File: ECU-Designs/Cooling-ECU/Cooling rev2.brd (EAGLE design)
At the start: 66.3 x 41.9 mm, 17 parts, among them T1 N-CHANNEL_MOSFETGENERIC, T2 N-CHANNEL_MOSFETGENERIC, T3 N-CHANNEL_MOSFETGENERIC, X1 MINIFIT_5566-12

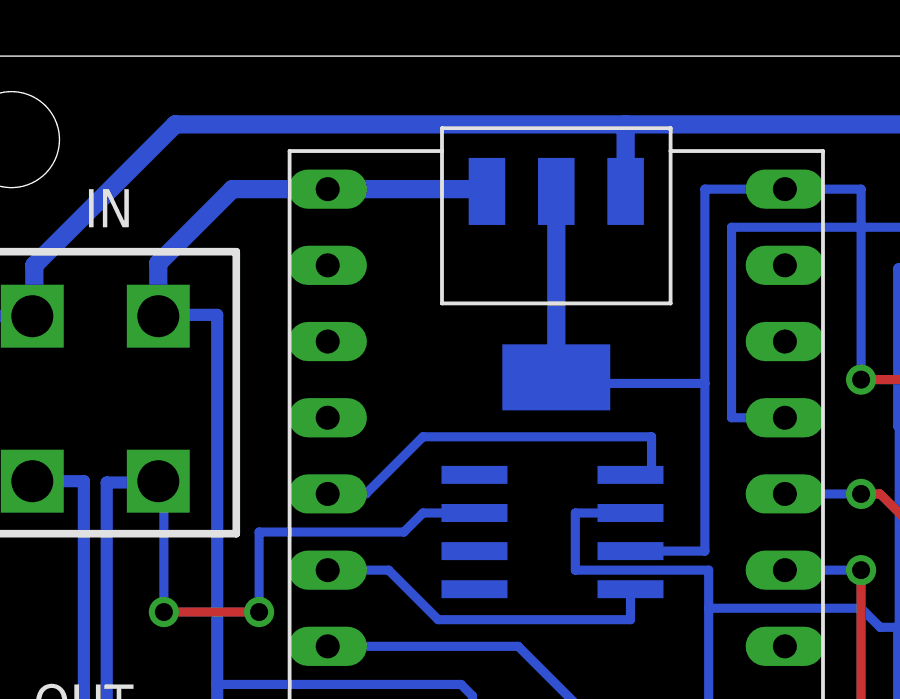
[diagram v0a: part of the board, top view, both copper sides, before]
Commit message: Tried milling out cooling board
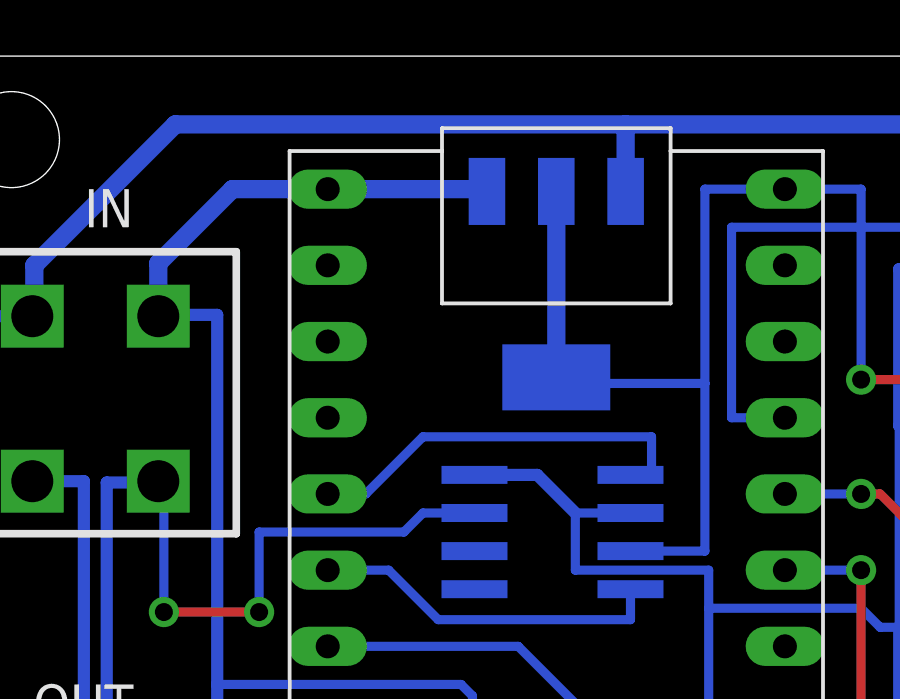
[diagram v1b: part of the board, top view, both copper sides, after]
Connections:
- net GND: now also U$2.8
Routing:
- net GND: track 194.4 -> 198.3 mm
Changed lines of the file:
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@@
 <?xml version="1.0" encoding="utf-8"?>
 <!DOCTYPE eagle SYSTEM "eagle.dtd">
-<eagle version="7.6.0">
+<eagle version="7.2.0">
 <drawing>
 <settings>
@@
 <wire x1="32.385" y1="34.798" x2="33.655" y2="34.798" width="0.4064" layer="16"/>
 <wire x1="33.655" y1="34.798" x2="33.655" y2="34.8996" width="0.4064" layer="16"/>
-<wire x1="13.335" y1="37.465" x2="13.97" y2="37.465" width="0.6096" layer="16"/>
-<wire x1="13.97" y1="37.465" x2="18.6436" y2="37.465" width="0.6096" layer="16"/>
+<wire x1="13.335" y1="37.465" x2="18.6436" y2="37.465" width="0.6096" layer="16"/>
 <wire x1="18.6436" y1="37.465" x2="18.6436" y2="37.3888" width="0.6096" layer="16"/>
 <wire x1="7.688" y1="16.72" x2="9.608" y2="16.72" width="0.4064" layer="16"/>
@@
 <wire x1="7.688" y1="34.993" x2="10.16" y2="37.465" width="0.6096" layer="16"/>
 <wire x1="10.16" y1="37.465" x2="13.335" y2="37.465" width="0.6096" layer="16"/>
+<contactref element="U$2" pad="8"/>
+<wire x1="18.228" y1="27.94" x2="20.32" y2="27.94" width="0.4064" layer="16"/>
+<wire x1="20.32" y1="27.94" x2="21.59" y2="26.67" width="0.4064" layer="16"/>
 </signal>
 <signal name="N$2">

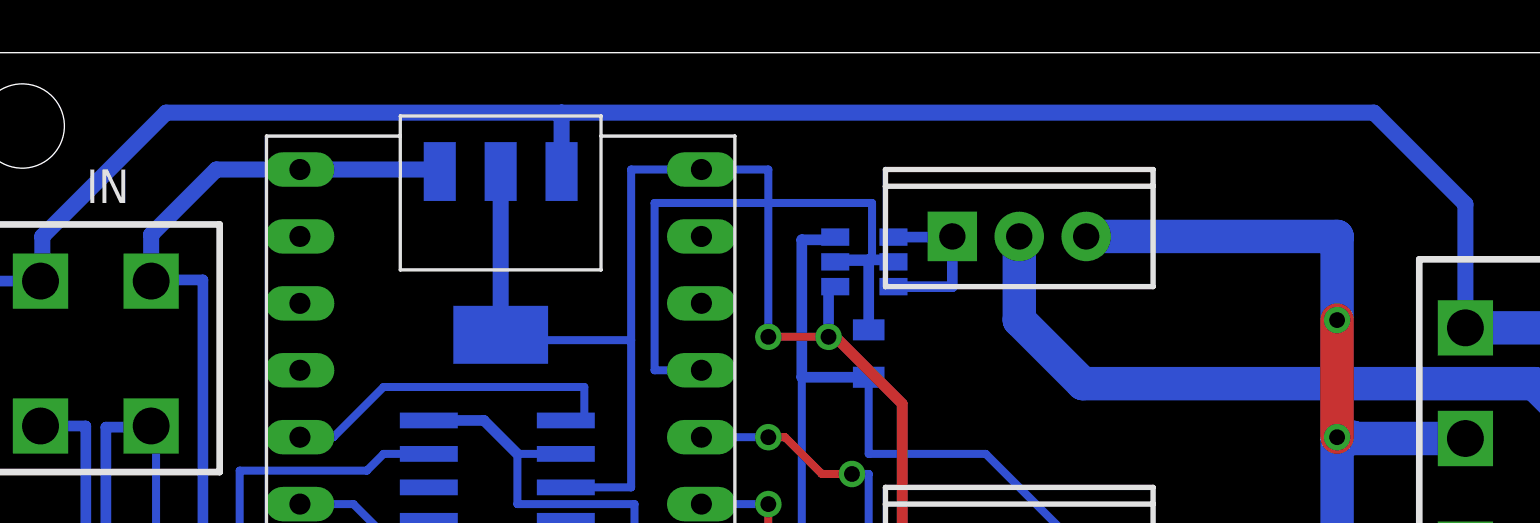
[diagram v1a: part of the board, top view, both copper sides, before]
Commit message: Nathan screwed up the package so we had to blow stuff up
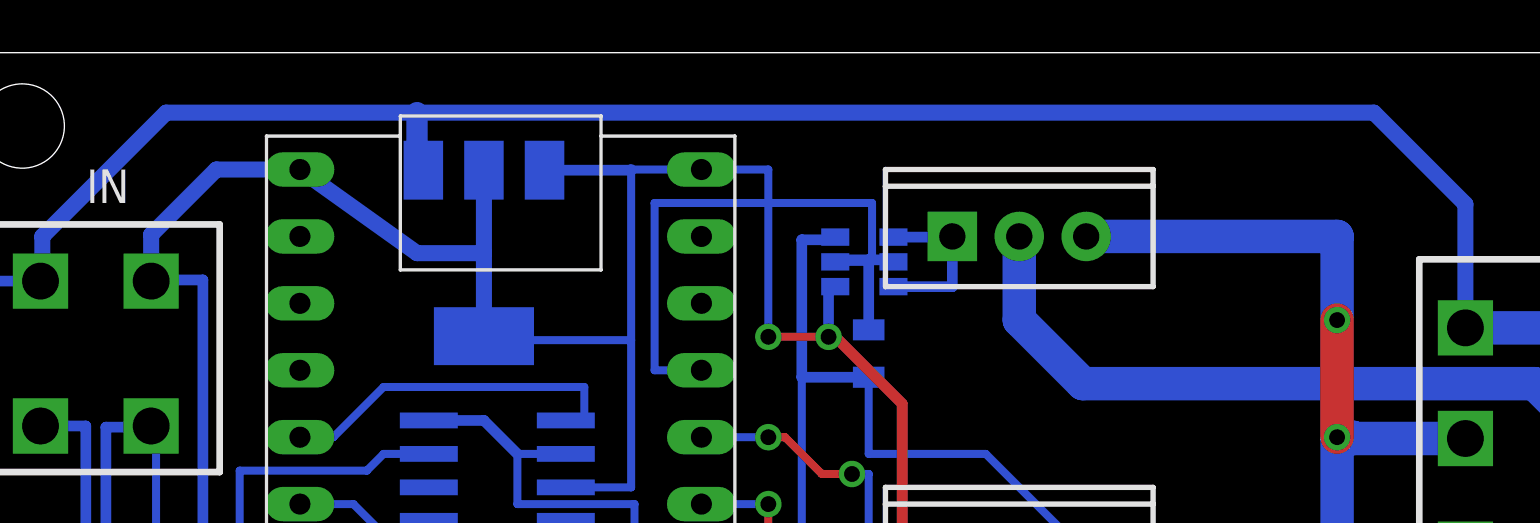
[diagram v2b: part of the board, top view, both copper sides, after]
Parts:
- removed 5V_REG: (no value), HyTechDevices:SOT223
- added U$4: (no value), HyTechDevices:SOT223
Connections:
- net +12V: now also U$4.1; no longer 5V_REG.3
- net +5V: now also U$4.3; no longer 5V_REG.2, 5V_REG.4
- net GND: now also U$4.2, U$4.4; no longer 5V_REG.1
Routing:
- net GND: track 198.3 -> 207.3 mm
- net +5V: track 119.2 -> 116.0 mm
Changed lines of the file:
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@@
 </autorouter>
 <elements>
-<element name="5V_REG" library="HyTechDevices" package="SOT223" value="" x="20.955" y="34.29" rot="MR180"/>
 <element name="IN" library="HyTechDevices" package="MINIFIT_5566-4" value="MINIFIT_5566-4" x="5.588" y="30.48" rot="R180">
 <attribute name="OC_FARNELL" value="unknown" x="5.588" y="30.48" size="1.778" layer="27" rot="R180" display="off"/>
@@
 <element name="G2" library="HyTechDevices" package="SOT23-6" value="GATE_DRIVEZXGD3003E6TA" x="33.655" y="20.955" rot="MR90"/>
 <element name="G3" library="HyTechDevices" package="SOT23-6" value="GATE_DRIVEZXGD3003E6TA" x="33.655" y="8.89" rot="MR90"/>
+<element name="U$4" library="HyTechDevices" package="SOT223" value="" x="20.32" y="34.29" rot="MR180"/>
 </elements>
 <signals>
 <signal name="GND">
-<contactref element="5V_REG" pad="1"/>
 <contactref element="IN" pad="2"/>
 <contactref element="OUT" pad="2"/>
@@
 <wire x1="32.385" y1="34.798" x2="33.655" y2="34.798" width="0.4064" layer="16"/>
 <wire x1="33.655" y1="34.798" x2="33.655" y2="34.8996" width="0.4064" layer="16"/>
-<wire x1="13.335" y1="37.465" x2="18.6436" y2="37.465" width="0.6096" layer="16"/>
-<wire x1="18.6436" y1="37.465" x2="18.6436" y2="37.3888" width="0.6096" layer="16"/>
+<wire x1="13.335" y1="37.465" x2="17.78" y2="34.29" width="0.6096" layer="16"/>
 <wire x1="7.688" y1="16.72" x2="9.608" y2="16.72" width="0.4064" layer="16"/>
 <wire x1="9.608" y1="16.72" x2="9.652" y2="16.764" width="0.4064" layer="16"/>
@@
 <wire x1="18.228" y1="27.94" x2="20.32" y2="27.94" width="0.4064" layer="16"/>
 <wire x1="20.32" y1="27.94" x2="21.59" y2="26.67" width="0.4064" layer="16"/>
+<contactref element="U$4" pad="4"/>
+<contactref element="U$4" pad="2"/>
+<wire x1="17.78" y1="34.29" x2="20.32" y2="34.29" width="0.6096" layer="16"/>
+<wire x1="20.32" y1="34.29" x2="20.32" y2="31.14" width="0.6096" layer="16"/>
+<wire x1="20.32" y1="34.29" x2="20.32" y2="37.44" width="0.6096" layer="16"/>
 </signal>
 <signal name="N$2">
@@
 </signal>
 <signal name="+5V">
-<contactref element="5V_REG" pad="2"/>
-<contactref element="5V_REG" pad="4"/>
 <contactref element="U$2" pad="3"/>
 <contactref element="U$3" pad="16"/>
@@
 <via x="33.401" y="6.604" extent="1-16" drill="0.6"/>
 <wire x1="33.655" y1="19.05" x2="33.655" y2="20.955" width="0.4064" layer="16"/>
-<wire x1="20.955" y1="31.191" x2="20.955" y2="37.3888" width="0.6096" layer="16"/>
 <wire x1="28.575" y1="37.465" x2="25.908" y2="37.465" width="0.3048" layer="16"/>
 <wire x1="25.908" y1="37.465" x2="25.908" y2="30.988" width="0.3048" layer="16"/>
 <wire x1="25.908" y1="30.988" x2="21.158" y2="30.988" width="0.3048" layer="16"/>
-<wire x1="21.158" y1="30.988" x2="20.955" y2="31.191" width="0.4064" layer="16"/>
 <wire x1="23.622" y1="6.985" x2="23.622" y2="3.683" width="0.4064" layer="16"/>
 <wire x1="23.622" y1="3.683" x2="25.4" y2="1.905" width="0.4064" layer="16"/>
@@
 <wire x1="54.61" y1="21.59" x2="54.84" y2="21.59" width="0.3048" layer="16"/>
 <wire x1="54.84" y1="21.59" x2="57.575" y2="18.855" width="0.3048" layer="16"/>
+<contactref element="U$4" pad="3"/>
+<wire x1="22.62" y1="37.44" x2="25.908" y2="37.44" width="0.4064" layer="16"/>
+<wire x1="25.908" y1="37.44" x2="25.908" y2="37.465" width="0.4064" layer="16"/>
 </signal>
 <signal name="N$1">
@@
 </signal>
 <signal name="+12V">
-<contactref element="5V_REG" pad="3"/>
 <contactref element="IN" pad="1"/>
 <contactref element="OUT" pad="1"/>
@@
 <wire x1="3.488" y1="16.764" x2="3.488" y2="16.72" width="0.4064" layer="16"/>
 <wire x1="3.488" y1="33.23" x2="3.556" y2="33.23" width="0.6096" layer="16"/>
-<wire x1="8.255" y1="39.624" x2="23.2664" y2="39.624" width="0.6096" layer="16"/>
-<wire x1="23.2664" y1="39.624" x2="23.2664" y2="37.3888" width="0.6096" layer="16"/>
 <wire x1="57.575" y1="31.455" x2="57.575" y2="36.151" width="0.6096" layer="16"/>
 <wire x1="57.575" y1="36.151" x2="54.102" y2="39.624" width="0.6096" layer="16"/>
-<wire x1="54.102" y1="39.624" x2="23.2664" y2="39.624" width="0.6096" layer="16"/>
+<wire x1="54.102" y1="39.624" x2="17.78" y2="39.624" width="0.6096" layer="16"/>
+<wire x1="17.78" y1="39.624" x2="8.255" y2="39.624" width="0.6096" layer="16"/>
 <wire x1="63.075" y1="14.655" x2="64.974" y2="14.655" width="1.27" layer="16"/>
 <wire x1="64.974" y1="14.655" x2="65.151" y2="14.605" width="1.27" layer="16"/>
@@
 <wire x1="3.556" y1="33.23" x2="3.556" y2="34.925" width="0.6096" layer="16"/>
 <wire x1="3.556" y1="34.925" x2="8.255" y2="39.624" width="0.6096" layer="16"/>
+<contactref element="U$4" pad="1"/>
+<wire x1="18.02" y1="37.44" x2="17.78" y2="37.44" width="0.4064" layer="16"/>
+<wire x1="17.78" y1="37.44" x2="17.78" y2="39.624" width="0.8128" layer="16"/>
 </signal>
 <signal name="FAN1-">
